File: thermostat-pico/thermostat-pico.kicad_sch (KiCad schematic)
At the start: 46 parts, among them J1 VAC IN, J2 Conn_01x06, J3 UART, U1 LY68L6400SLIT, U2 ESP32-PICO-D4, U4 TPS5430DDA, U5 TPS5430DDA, U6 LM324DT

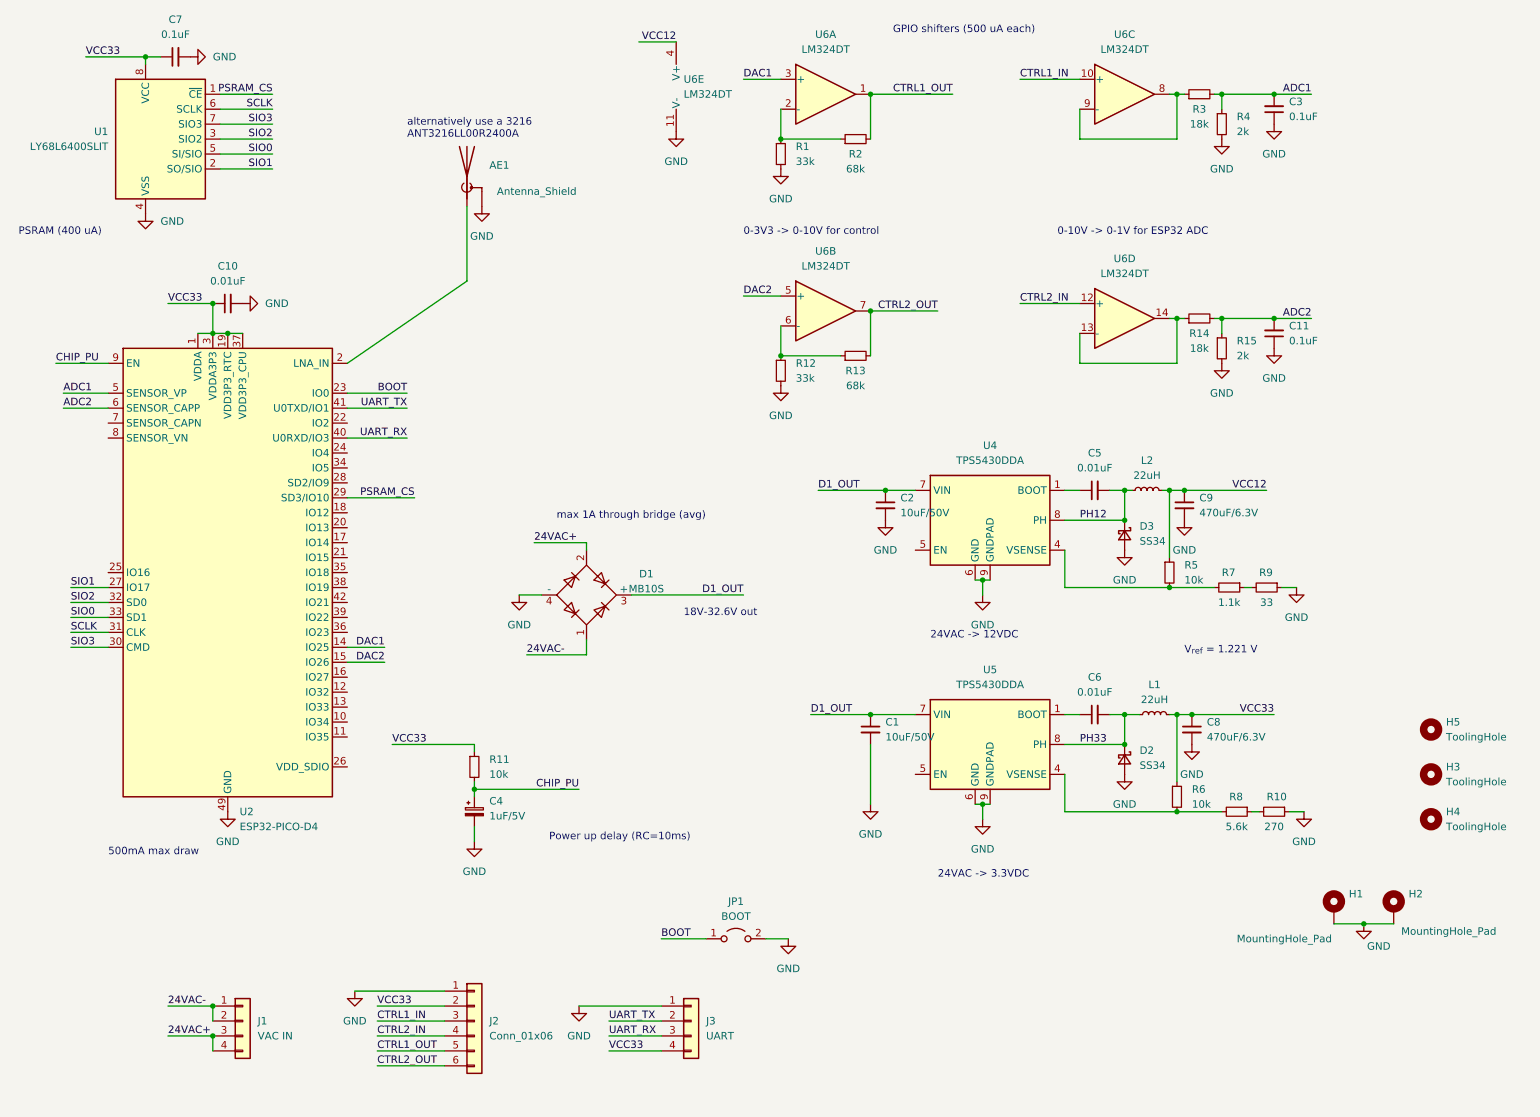
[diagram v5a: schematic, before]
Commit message: Update tracks, add inductor 3D model
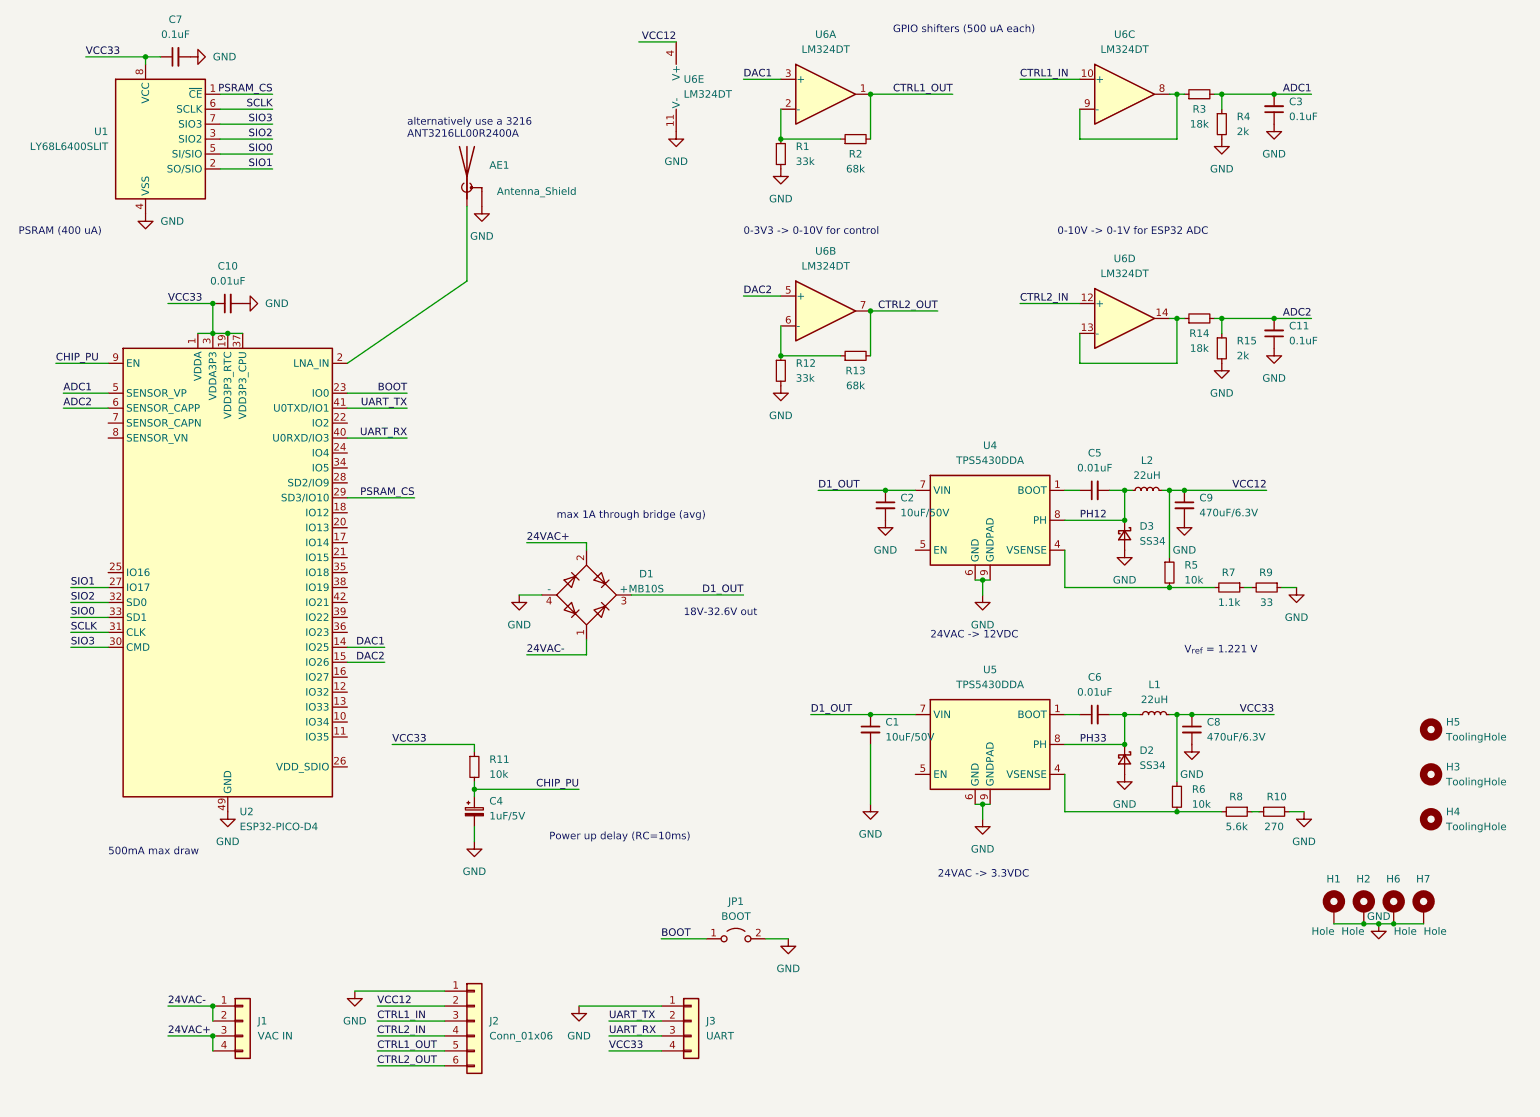
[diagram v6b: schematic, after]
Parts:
- added H6, H7: Hole, MountingHole:MountingHole_2.2mm_M2_DIN965_Pad, symbol Mechanical:MountingHole_Pad
- AE1: footprint RF_Antenna:Texas_SWRA117D_2.4GHz_Left -> kelvie:Texas_SWRA117D_2.4GHz_Right
- H1, H2: value MountingHole_Pad -> Hole
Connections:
- net GND: now also H6.1, H7.1
- net VCC12: now also J2.2 (Pin_2)
- net VCC33: no longer J2.2 (Pin_2)
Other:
- moved on the sheet: H2
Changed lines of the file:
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@@
   (junction (at 217.17 64.77) (diameter 0) (color 0 0 0 0)
   )
+  (junction (at 246.38 167.64) (diameter 0) (color 0 0 0 0)
+  )
   (junction (at 142.24 71.12) (diameter 0) (color 0 0 0 0)
   )
@@
   (junction (at 45.72 62.23) (diameter 0) (color 0 0 0 0)
   )
+  (junction (at 243.84 167.64) (diameter 0) (color 0 0 0 0)
+  )
   (junction (at 157.48 63.5) (diameter 0) (color 0 0 0 0)
   )
@@
     (stroke (width 0) (type default) (color 0 0 0 0))
   )
-  (wire (pts (xy 100.33 102.87) (xy 109.22 102.87))
+  (wire (pts (xy 99.06 102.87) (xy 109.22 102.87))
     (stroke (width 0) (type default) (color 0 0 0 0))
   )
@@
     (stroke (width 0) (type default) (color 0 0 0 0))
   )
+  (wire (pts (xy 243.84 167.64) (xy 246.38 167.64))
+    (stroke (width 0) (type default) (color 0 0 0 0))
+  )
   (wire (pts (xy 88.9 58.42) (xy 68.58 72.39))
     (stroke (width 0) (type default) (color 0 0 0 0))
@@
     (stroke (width 0) (type default) (color 0 0 0 0))
   )
-  (wire (pts (xy 241.3 167.64) (xy 246.38 167.64))
-    (stroke (width 0) (type default) (color 0 0 0 0))
-  )
   (wire (pts (xy 203.2 132.08) (xy 200.66 132.08))
     (stroke (width 0) (type default) (color 0 0 0 0))
@@
     (stroke (width 0) (type default) (color 0 0 0 0))
   )
+  (wire (pts (xy 246.38 167.64) (xy 251.46 167.64))
+    (stroke (width 0) (type default) (color 0 0 0 0))
+  )
   (wire (pts (xy 68.58 120.65) (xy 74.93 120.65))
     (stroke (width 0) (type default) (color 0 0 0 0))
@@
     (stroke (width 0) (type default) (color 0 0 0 0))
   )
+  (wire (pts (xy 241.3 167.64) (xy 243.84 167.64))
+    (stroke (width 0) (type default) (color 0 0 0 0))
+  )
   (wire (pts (xy 107.95 181.61) (xy 121.92 181.61))
     (stroke (width 0) (type default) (color 0 0 0 0))
@@
     (effects (font (size 1.27 1.27)) (justify left bottom))
   )
-  (label "24VAC+" (at 100.33 102.87 0)
+  (label "24VAC+" (at 99.06 102.87 0)
     (effects (font (size 1.27 1.27)) (justify left bottom))
   )
@@
     (effects (font (size 1.27 1.27)) (justify right bottom))
   )
-  (label "VCC33" (at 73.66 181.61 0)
+  (label "VCC12" (at 73.66 181.61 0)
     (effects (font (size 1.27 1.27)) (justify left bottom))
   )
@@
       (effects (font (size 1.27 1.27)) (justify left))
     )
-    (property "Footprint" "RF_Antenna:Texas_SWRA117D_2.4GHz_Left" (id 2) (at 88.9 38.1 0)
+    (property "Footprint" "kelvie:Texas_SWRA117D_2.4GHz_Right" (id 2) (at 88.9 38.1 0)
       (effects (font (size 1.27 1.27)) hide)
     )
@@
     (pin "6")
   )
+  (symbol (lib_id "Mechanical:MountingHole_Pad") (at 246.38 165.1 0) (unit 1)
+    (in_bom yes) (on_board yes)
+    (property "Reference" "H6" (id 0) (at 245.11 160.02 0)
+      (effects (font (size 1.27 1.27)) (justify left))
+    )
+    (property "Value" "Hole" (id 1) (at 237.49 168.91 0)
+      (effects (font (size 1.27 1.27)) (justify left))
+    )
+    (property "Footprint" "MountingHole:MountingHole_2.2mm_M2_DIN965_Pad" (id 2) (at 246.38 165.1 0)
+      (effects (font (size 1.27 1.27)) hide)
+    )
+    (property "Datasheet" "~" (id 3) (at 246.38 165.1 0)
+      (effects (font (size 1.27 1.27)) hide)
+    )
+    (pin "1")
+  )
   (symbol (lib_id "Device:C_Small") (at 39.37 20.32 90) (unit 1)
     (in_bom yes) (on_board yes) (fields_autoplaced)
@@
   (symbol (lib_id "Mechanical:MountingHole_Pad") (at 236.22 165.1 0) (unit 1)
     (in_bom yes) (on_board yes)
-    (property "Reference" "H1" (id 0) (at 238.76 162.5599 0)
-      (effects (font (size 1.27 1.27)) (justify left))
-    )
-    (property "Value" "MountingHole_Pad" (id 1) (at 219.71 170.18 0)
+    (property "Reference" "H1" (id 0) (at 234.95 160.02 0)
+      (effects (font (size 1.27 1.27)) (justify left))
+    )
+    (property "Value" "Hole" (id 1) (at 232.41 168.91 0)
       (effects (font (size 1.27 1.27)) (justify left))
     )
@@
     (pin "2")
   )
-  (symbol (lib_id "Mechanical:MountingHole_Pad") (at 246.38 165.1 0) (unit 1)
+  (symbol (lib_id "Mechanical:MountingHole_Pad") (at 241.3 165.1 0) (unit 1)
     (in_bom yes) (on_board yes)
-    (property "Reference" "H2" (id 0) (at 248.92 162.5599 0)
-      (effects (font (size 1.27 1.27)) (justify left))
-    )
-    (property "Value" "MountingHole_Pad" (id 1) (at 247.65 168.91 0)
-      (effects (font (size 1.27 1.27)) (justify left))
-    )
-    (property "Footprint" "MountingHole:MountingHole_2.2mm_M2_DIN965_Pad" (id 2) (at 246.38 165.1 0)
-      (effects (font (size 1.27 1.27)) hide)
-    )
-    (property "Datasheet" "~" (id 3) (at 246.38 165.1 0)
+    (property "Reference" "H2" (id 0) (at 240.03 160.02 0)
+      (effects (font (size 1.27 1.27)) (justify left))
+    )
+    (property "Value" "Hole" (id 1) (at 246.38 168.91 0)
+      (effects (font (size 1.27 1.27)) (justify left))
+    )
+    (property "Footprint" "MountingHole:MountingHole_2.2mm_M2_DIN965_Pad" (id 2) (at 241.3 165.1 0)
+      (effects (font (size 1.27 1.27)) hide)
+    )
+    (property "Datasheet" "~" (id 3) (at 241.3 165.1 0)
       (effects (font (size 1.27 1.27)) hide)
     )
@@
     (pin "2")
   )
-  (symbol (lib_id "power:GND") (at 241.3 167.64 0) (unit 1)
+  (symbol (lib_id "power:GND") (at 243.84 167.64 0) (unit 1)
     (in_bom yes) (on_board yes)
-    (property "Reference" "#PWR0105" (id 0) (at 241.3 173.99 0)
-      (effects (font (size 1.27 1.27)) hide)
-    )
-    (property "Value" "GND" (id 1) (at 243.84 171.45 0))
-    (property "Footprint" "" (id 2) (at 241.3 167.64 0)
-      (effects (font (size 1.27 1.27)) hide)
-    )
-    (property "Datasheet" "" (id 3) (at 241.3 167.64 0)
+    (property "Reference" "#PWR0105" (id 0) (at 243.84 173.99 0)
+      (effects (font (size 1.27 1.27)) hide)
+    )
+    (property "Value" "GND" (id 1) (at 243.84 166.37 0))
+    (property "Footprint" "" (id 2) (at 243.84 167.64 0)
+      (effects (font (size 1.27 1.27)) hide)
+    )
+    (property "Datasheet" "" (id 3) (at 243.84 167.64 0)
       (effects (font (size 1.27 1.27)) hide)
     )
@@
     (pin "2")
   )
+  (symbol (lib_id "Mechanical:MountingHole_Pad") (at 251.46 165.1 0) (unit 1)
+    (in_bom yes) (on_board yes)
+    (property "Reference" "H7" (id 0) (at 250.19 160.02 0)
+      (effects (font (size 1.27 1.27)) (justify left))
+    )
+    (property "Value" "Hole" (id 1) (at 251.46 168.91 0)
+      (effects (font (size 1.27 1.27)) (justify left))
+    )
+    (property "Footprint" "MountingHole:MountingHole_2.2mm_M2_DIN965_Pad" (id 2) (at 251.46 165.1 0)
+      (effects (font (size 1.27 1.27)) hide)
+    )
+    (property "Datasheet" "~" (id 3) (at 251.46 165.1 0)
+      (effects (font (size 1.27 1.27)) hide)
+    )
+    (pin "1")
+  )
   (symbol (lib_id "Jumper:Jumper_2_Open") (at 134.62 170.18 0) (unit 1)
     (in_bom yes) (on_board yes) (fields_autoplaced)
@@
     )
     (path "/4152d3bb-c041-4427-a63d-81906847f9dc"
-      (reference "AE1") (unit 1) (value "Antenna_Shield") (footprint "RF_Antenna:Texas_SWRA117D_2.4GHz_Left")
+      (reference "AE1") (unit 1) (value "Antenna_Shield") (footprint "kelvie:Texas_SWRA117D_2.4GHz_Right")
     )
     (path "/a150ca98-7276-4ad9-a256-bbbdafe86ad0"
@@
     )
     (path "/66af7211-cc92-401d-ab2c-04040d051a86"
-      (reference "H1") (unit 1) (value "MountingHole_Pad") (footprint "MountingHole:MountingHole_2.2mm_M2_DIN965_Pad")
+      (reference "H1") (unit 1) (value "Hole") (footprint "MountingHole:MountingHole_2.2mm_M2_DIN965_Pad")
     )
     (path "/7230bef0-ba3e-42ff-ac34-80bd8b4ffb83"
-      (reference "H2") (unit 1) (value "MountingHole_Pad") (footprint "MountingHole:MountingHole_2.2mm_M2_DIN965_Pad")
+      (reference "H2") (unit 1) (value "Hole") (footprint "MountingHole:MountingHole_2.2mm_M2_DIN965_Pad")
     )
     (path "/9ef5e703-a32f-4d55-916d-f0b78eccaca2"
@@
       (reference "H5") (unit 1) (value "ToolingHole") (footprint "kelvie:ToolingHole_1.152mm")
     )
+    (path "/5e461c6c-2819-4853-b380-27eecb23a120"
+      (reference "H6") (unit 1) (value "Hole") (footprint "MountingHole:MountingHole_2.2mm_M2_DIN965_Pad")
+    )
+    (path "/f9f2cef2-06d0-4aff-a0a8-38067bf95803"
+      (reference "H7") (unit 1) (value "Hole") (footprint "MountingHole:MountingHole_2.2mm_M2_DIN965_Pad")
+    )
     (path "/f1534488-0c57-4f37-9331-650460480fa5"
